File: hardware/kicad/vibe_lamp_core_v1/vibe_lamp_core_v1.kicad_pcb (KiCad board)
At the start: 2 copper layers, 32 x 32 mm, 27 parts, among them J1 USB-C_SMD-TYPE-C-31-M-12_1, P1 PinHeader_1x03_P2.54mm_Vertic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, SW1 Panasonic_EVQPUJ_EVQPUA, U1 WIFIM-SMD_ESP32-C3-MINI-1, U2 SOT-25-5_L2.9-W1.6-P0.95-LS2.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

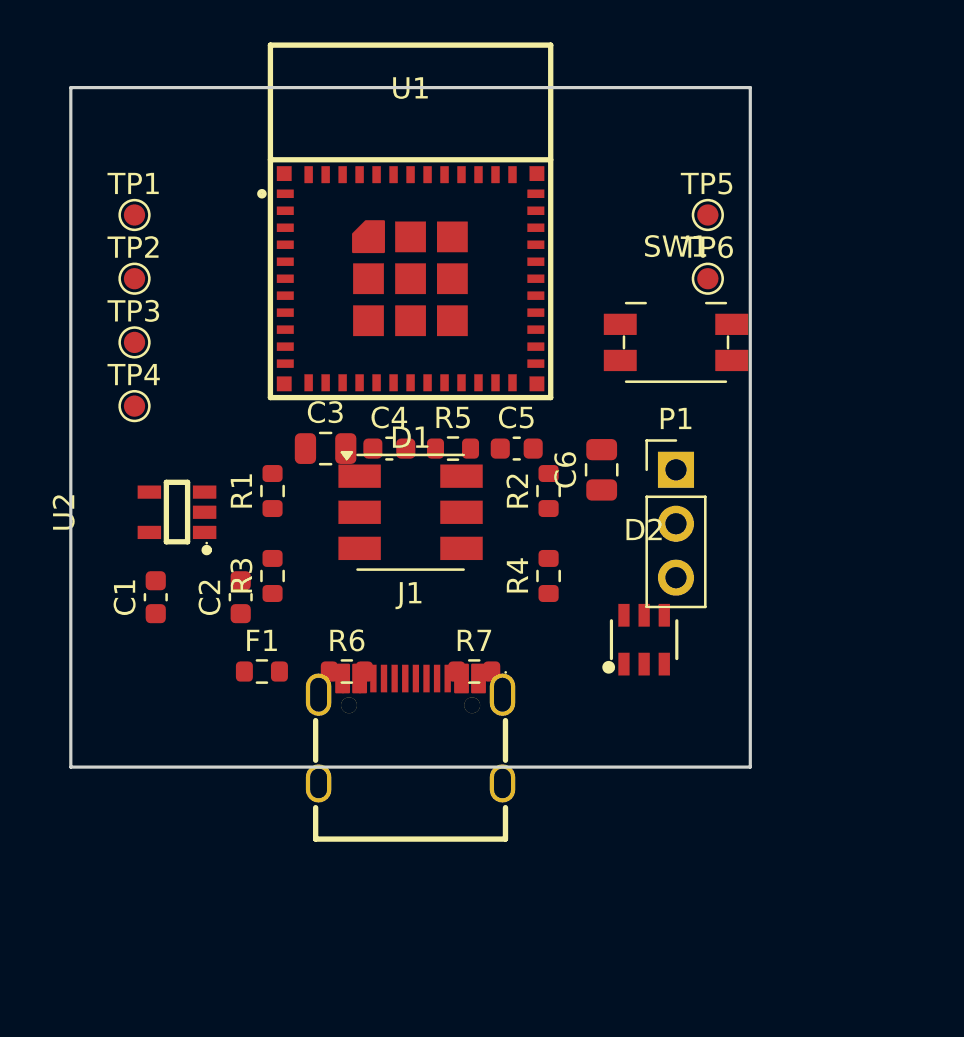
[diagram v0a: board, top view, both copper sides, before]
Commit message: wip(hardware): Core V1 auto-routed draft (Freerouting) + routing status
Auto-routed the placed board with Freerouting v1.9.0 (~75%, 64/86 connections) + dual-layer GND pour. NOT fab-ready: 21 unrouted, 4 shorts, 17 antenna-keepout intrusions, 9 courtyard overlaps remain (see hardware/v1_routing_status.md). Reproducible pcbnew/DSN/SES scripts saved under scripts/. The clean placed+netlist base is commit 9fb418d.

Co-Authored-By: Claude Opus 4.8 (1M context) <noreply@anthropic.com>
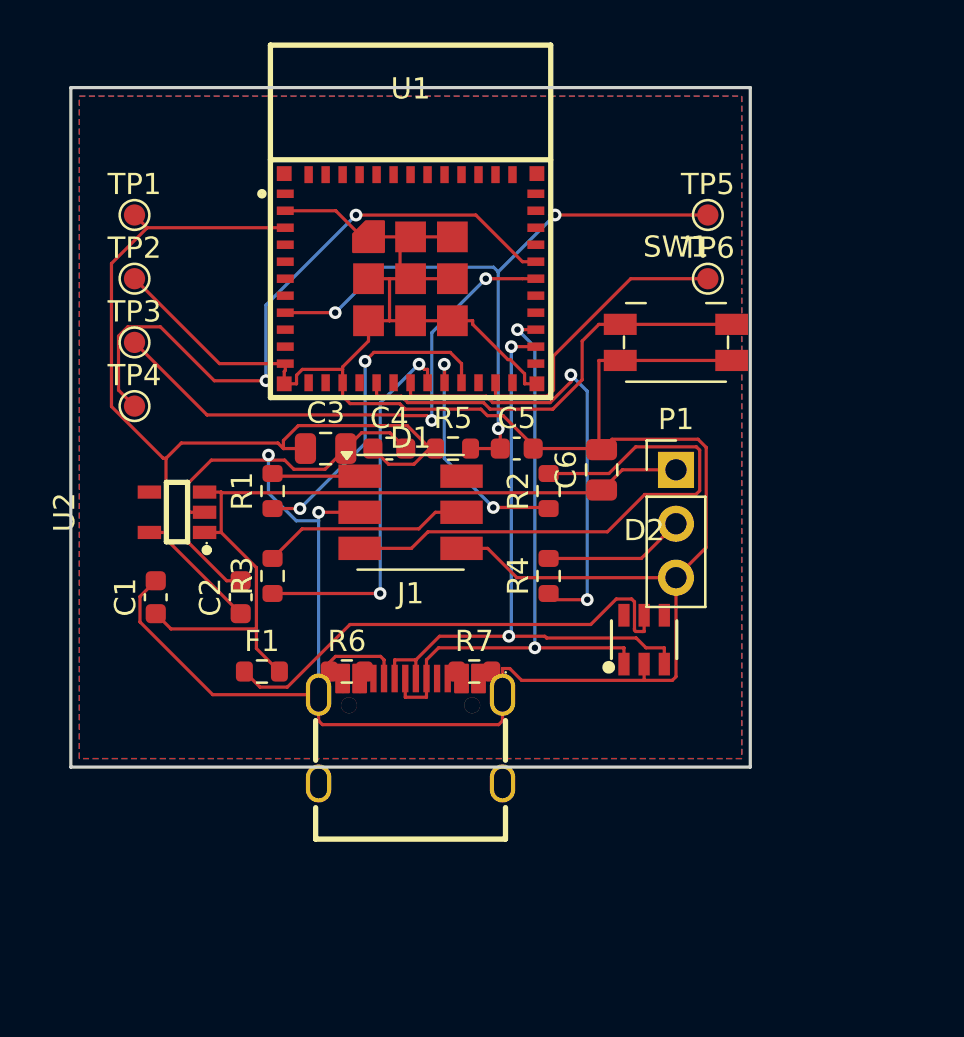
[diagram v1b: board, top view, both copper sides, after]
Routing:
- net GND: track 0.00 -> 163.3 mm, vias 0 -> 2
- net +3V3: track 0.00 -> 48.2 mm
- net +5V: track 0.00 -> 38.1 mm
- net EN: track 0.00 -> 31.7 mm, vias 0 -> 3
- net USB_DM: track 0.00 -> 30.8 mm, vias 0 -> 2
- net UART_TX: track 0.00 -> 30.7 mm, vias 0 -> 2
- net USB_DP: track 0.00 -> 30.1 mm, vias 0 -> 2
- net RGB_G: track 0.00 -> 26.8 mm
- net UART_RX: track 0.00 -> 25.6 mm, vias 0 -> 2
- net VBUS: track 0.00 -> 23.0 mm
- net IO4: track 0.00 -> 21.9 mm, vias 0 -> 2
- net BTN: track 0.00 -> 20.3 mm
- net IO5: track 0.00 -> 17.8 mm, vias 0 -> 2
- net IO7: track 0.00 -> 15.3 mm, vias 0 -> 2
- net IO9: track 0.00 -> 13.9 mm
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- added copper zone on B.Cu, net GND
- added copper zone on F.Cu, net GND

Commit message: feat(hardware): Core V1 clean 40x40 routed board (0 shorts, 1 unrouted)
Re-laid out on a 40x40 board with proper spacing and re-routed with Freerouting (100 passes) + dual-layer GND pour. From 86 violations/21 unconnected/4 shorts down to 23 violations/1 unconnected/0 shorts. Remaining are minor/tunable (tight clearances, GND thermals, silk, 1 unrouted net). Near fab-ready; final cleanup = relax clearance to JLCPCB spec, route 1 net, thermal tweak, then Gerber/BOM/CPL. See hardware/v1_routing_status.md.

Co-Authored-By: Claude Opus 4.8 (1M context) <noreply@anthropic.com>
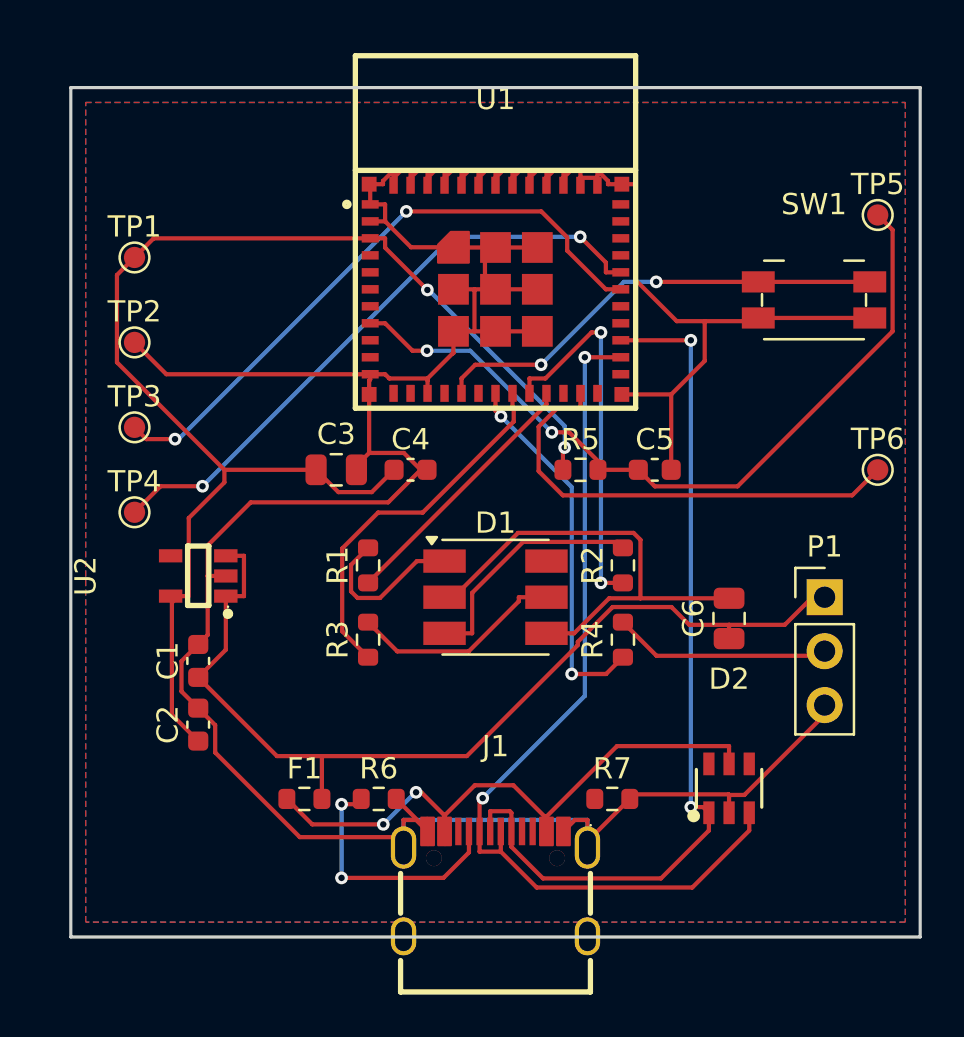
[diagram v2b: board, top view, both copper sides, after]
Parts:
- moved TP6 12.0 mm to (38.0, 18.0)
- moved C6 9.22 mm to (31.0, 25.0)
- moved P1 9.22 mm to (35.5, 24.0)
- moved R7 8.85 mm to (25.5, 33.5)
- moved J1 8.24 mm to (20.0, 37.5)
- moved D2 8.06 mm to (31.0, 33.0)
- moved TP5 8.00 mm to (38.0, 6.00)
- moved SW1 6.80 mm to (35.0, 10.0)
- moved C5 6.58 mm to (27.5, 18.0)
- moved C2 6.32 mm to (6.00, 30.0)
- moved F1 6.32 mm to (11.0, 33.5)
- moved R6 6.18 mm to (14.5, 33.5)
- moved R5 6.08 mm to (24.0, 18.0)
- moved R1 5.70 mm to (14.0, 22.5)
- moved D1 5.66 mm to (20.0, 24.0)
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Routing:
- net GND: track 163.3 -> 189.0 mm, vias 2 -> 0
- net RGB_G: track 26.8 -> 11.4 mm
- net +3V3: track 48.2 -> 62.9 mm, vias 0 -> 2
- net USB_DM: track 30.8 -> 43.3 mm
- net USB_DP: track 30.1 -> 41.5 mm
- net IO9: track 13.9 -> 22.1 mm
- net CC1: track 4.07 -> 12.0 mm, vias 0 -> 2
- net +5V: track 38.1 -> 45.6 mm
- net IO6: track 11.2 -> 17.8 mm
- net EN: track 31.7 -> 36.8 mm, vias 3 -> 2
- net IO4: track 21.9 -> 17.4 mm
- net VBUS: track 23.0 -> 27.3 mm, vias 0 -> 2
- net UART_RX: track 25.6 -> 29.5 mm
- net WS_DATA: track 6.68 -> 10.2 mm
- net RGB_R: track 4.15 -> 7.64 mm
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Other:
- board size 32 x 32 mm -> 40 x 40 mm

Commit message: feat(hardware): Core V1 fab outputs (Gerber/drill/BOM/CPL) + component values
Set real component values; export JLCPCB-ready Gerber+drill zip, BOM (U1/U2/J1/D2 with LCSC), and CPL placement under fab/. Board is 0 shorts, 1 unrouted net (CC2) — a draft; see v1_routing_status.md for the pre-order checklist (route CC2, fill passive LCSC, clear connector-inherent DRC).

Co-Authored-By: Claude Opus 4.8 (1M context) <noreply@anthropic.com>
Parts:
- C1, C2: value C_0603_1608Metric -> 1uF
- C3: value C_0805_2012Metric -> 10uF
- C4, C5: value C_0603_1608Metric -> 100nF
- C6: value C_0805_2012Metric -> 470uF
- D1: value LED_RGB_5050-6 -> RGB-LED-5050-CC
- D2: value SOT-23-6_L2.9-W1.6-P0.95-LS2.8-BL -> USBLC6-2SC6
- F1: value R_0603_1608Metric -> 0R
- J1: value USB-C_SMD-TYPE-C-31-M-12_1 -> USB-C-TYPE-C-31-M-12
- P1: value PinHeader_1x03_P2.54mm_Vertical -> WS2812-EXT-1x3
- R1: value R_0603_1608Metric -> 470
- R2, R3: value R_0603_1608Metric -> 150
- R4: value R_0603_1608Metric -> 330
- R5: value R_0603_1608Metric -> 10k
- R6, R7: value R_0603_1608Metric -> 5.1k
- SW1: value Panasonic_EVQPUJ_EVQPUA -> SW-PUSH
- U1: value WIFIM-SMD_ESP32-C3-MINI-1 -> ESP32-C3-MINI-1
- U2: value SOT-25-5_L2.9-W1.6-P0.95-LS2.8-BL -> AP2112K-3.3
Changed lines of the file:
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@@
 			)
 		)
-		(property "Value" "PinHeader_1x03_P2.54mm_Vertical"
+		(property "Value" "WS2812-EXT-1x3"
 			(at 0 7.46 0)
 			(layer "F.Fab")
@@
 			)
 		)
-		(property "Value" "R_0603_1608Metric"
+		(property "Value" "5.1k"
 			(at 0 1.43 0)
 			(layer "F.Fab")
@@
 			)
 		)
-		(property "Value" "C_0603_1608Metric"
+		(property "Value" "1uF"
 			(at 0 1.43 90)
 			(layer "F.Fab")
@@
 			)
 		)
-		(property "Value" "C_0805_2012Metric"
+		(property "Value" "470uF"
 			(at 0 1.68 90)
 			(layer "F.Fab")
@@
 			)
 		)
-		(property "Value" "C_0603_1608Metric"
+		(property "Value" "100nF"
 			(at 0 1.43 0)
 			(layer "F.Fab")
@@
 			)
 		)
-		(property "Value" "R_0603_1608Metric"
+		(property "Value" "0R"
 			(at 0 1.43 0)
 			(layer "F.Fab")
@@
 			)
 		)
-		(property "Value" "C_0603_1608Metric"
+		(property "Value" "1uF"
 			(at 0 1.43 90)
 			(layer "F.Fab")
@@
 			)
 		)
-		(property "Value" "SOT-25-5_L2.9-W1.6-P0.95-LS2.8-BL"
+		(property "Value" "AP2112K-3.3"
 			(at 0 5.3 90)
 			(layer "F.Fab")
@@
 			)
 		)
-		(property "Value" "R_0603_1608Metric"
+		(property "Value" "150"
 			(at 0 1.43 90)
 			(layer "F.Fab")
@@
 			)
 		)
-		(property "Value" "R_0603_1608Metric"
+		(property "Value" "10k"
 			(at 0 1.43 0)
 			(layer "F.Fab")
@@
 			)
 		)
-		(property "Value" "LED_RGB_5050-6"
+		(property "Value" "RGB-LED-5050-CC"
 			(at 0 3.3 0)
 			(layer "F.Fab")
@@
 			)
 		)
-		(property "Value" "C_0805_2012Metric"
+		(property "Value" "10uF"
 			(at 0 1.68 0)
 			(layer "F.Fab")
@@
 			)
 		)
-		(property "Value" "C_0603_1608Metric"
+		(property "Value" "100nF"
 			(at 0 1.43 0)
 			(layer "F.Fab")
@@
 			)
 		)
-		(property "Value" "USB-C_SMD-TYPE-C-31-M-12_1"
+		(property "Value" "USB-C-TYPE-C-31-M-12"
 			(at 0 6.474 0)
 			(layer "F.Fab")
@@
 			)
 		)
-		(property "Value" "SOT-23-6_L2.9-W1.6-P0.95-LS2.8-BL"
+		(property "Value" "USBLC6-2SC6"
 			(at 0 5.149 0)
 			(layer "F.Fab")
@@
 			)
 		)
-		(property "Value" "WIFIM-SMD_ESP32-C3-MINI-1"
+		(property "Value" "ESP32-C3-MINI-1"
 			(at 0 8.95 0)
 			(layer "F.Fab")
@@
 			)
 		)
-		(property "Value" "R_0603_1608Metric"
+		(property "Value" "150"
 			(at 0 1.43 90)
 			(layer "F.Fab")
@@
 			)
 		)
-		(property "Value" "R_0603_1608Metric"
+		(property "Value" "470"
 			(at 0 1.43 90)
 			(layer "F.Fab")
@@
 			)
 		)
-		(property "Value" "R_0603_1608Metric"
+		(property "Value" "330"
 			(at 0 1.43 90)
 			(layer "F.Fab")
@@
 			)
 		)
-		(property "Value" "R_0603_1608Metric"
+		(property "Value" "5.1k"
 			(at 0 1.43 0)
 			(layer "F.Fab")
@@
 			)
 		)
-		(property "Value" "Panasonic_EVQPUJ_EVQPUA"
+		(property "Value" "SW-PUSH"
 			(at 0 3.5 0)
 			(layer "F.Fab")

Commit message: feat(hardware): route CC2, fix USB-C edge fit, add "vibe lamp" silk, fab re-export
Core V1 PCB finishing pass — board is now electrically complete:
- CC2 routed: moved R7 (CC2 pulldown) into the clear lane due-north of
  J1.B5 so CC2 is a straight 1.41mm trace (Freerouting deprioritized it).
  scripts/route_cc2.py auto-adds it. Result: 0 shorts, 0 unconnected.
- J1 (USB-C) shifted up 1.2mm so all pads sit on-board (shell still
  overhangs the edge for cable insertion); opened the connector fan-out
  pocket to ~3.8mm by moving the bottom passive row up.
- Branding silkscreen "vibe lamp" on front + back, "v1" on back.
- Design rules set to JLCPCB process (copper-to-edge 0.2mm, clearance
  0.127mm). DRC: 0 short / 0 unconnected / 20 minor (10 USB-C connector
  -inherent + 8 cosmetic silk + courtyard + thermal).
- Re-exported all fab outputs; fixed gerber zip to include the actual
  manufacturing layers (copper/mask/silk/edge/paste/drill) — the prior
  zip glob (*.gbr) had silently dropped them. Dropped non-fab layers.
- BOM: verified LCSC parts against JLCPCB library. U1/U2/J1/D2 filled.
  D1 needs a selection decision (6-pin 5050 analog CC RGB has no clean
  JLCPCB stock match — see v1_routing_status.md); SW1 + passives guided.

Co-Authored-By: Claude Opus 4.8 (1M context) <noreply@anthropic.com>
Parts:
- moved R7 4.20 mm to (21.8, 31.6), turned to 90 degrees
- moved R6 3.81 mm to (13.0, 30.0)
- moved F1 3.64 mm to (10.0, 30.0)
- moved D2 3.00 mm to (31.0, 30.0)
- moved J1 1.20 mm to (20.0, 36.3)
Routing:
- net GND: track 189.0 -> 248.9 mm, vias 0 -> 1
- net UART_TX: track 29.2 -> 45.1 mm, vias 2 -> 0
- net EN: track 36.8 -> 44.8 mm
- net +3V3: track 62.9 -> 56.0 mm, vias 2 -> 0
- net IO4: track 17.4 -> 24.3 mm
- net BTN: track 21.8 -> 28.1 mm
- net IO9: track 22.1 -> 15.9 mm
- net IO5: track 17.5 -> 22.5 mm, vias 0 -> 2
- net IO6: track 17.8 -> 13.8 mm
- net RGB_R: track 7.64 -> 3.86 mm
- net UART_RX: track 29.5 -> 26.0 mm
- net IO7: track 12.4 -> 15.0 mm, vias 0 -> 2
- net USB_DP: track 41.5 -> 39.4 mm
- net CC1: track 12.0 -> 13.5 mm
- net CC2: track 0.00 -> 1.41 mm
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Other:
- board text added: "v1"
- board text added: "vibe lamp"

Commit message: feat(hardware,firmware): switch D1 to WS2812B, finalize Core V1 BOM
D1 part-selection decision: 6-pin analog 5050 common-cathode RGB has no
in-stock JLCPCB match, so switch the onboard LED to WS2812B (digital).

Hardware (Core V1 PCB):
- D1 -> WS2812B (LCSC C2761795, SMD5050-4P, 550k stock). Imported exact
  footprint via easyeda2kicad; pinout verified VDD/DOUT/VSS/DIN.
- Data chain GPIO4 -> R4(330) -> D1.DIN; D1.DOUT -> P1 (onboard LED is
  chain head, P1 cascades an external strip).
- Removed R1/R2/R3 (no RGB current-limit needed); added C7 100nF decap.
- SW1 -> SKRPABE010 (LCSC C115360) with its exact imported footprint.
- ESP32-C3-MINI-1 module pin->GPIO map verified against symbol: pin16=IO10
  (button), pin18=IO4 (WS data), pin26/27=IO18/19 (USB D-/D+), 3V3/EN/GND
  all correct.
- DRC: 0 short / 0 unconnected / 18 minor (10 USB-C connector-inherent +
  8 cosmetic silk). Rules set to JLCPCB process incl. min_resolved_spokes=1.
- Re-exported gerber/drill/cpl; BOM now has 6/6 key LCSC parts filled
  (U1/U2/J1/D2/D1/SW1); C6/P1 marked DNP; passives auto-match basic lib.

Firmware (additive, does NOT touch the working analog dev board):
- New env c3_core_v1: WS2812 single-LED (DISPLAY_WS2812_STRIP, NUM_LEDS=1,
  PIN_WS2812=4, PIN_RESET_BTN=10). Builds clean.
- config.h: make NUM_LEDS overridable via -DNUM_LEDS.
- Existing c3_rgb (analog RGB on GPIO5/6/7) unchanged; verified still builds.

Co-Authored-By: Claude Opus 4.8 (1M context) <noreply@anthropic.com>
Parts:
- removed R1: 470, R_0603_1608Metric
- removed R2, R3: 150, R_0603_1608Metric
- added C7: 100nF, C_0603_1608Metric, F.Cu at (14.0, 24.0)
- D1: value RGB-LED-5050-CC -> WS2812B; footprint LED_RGB_5050-6 -> LED-SMD_4P-L5.0-W5.0-TL_WS2812B-B
- SW1: footprint Panasonic_EVQPUJ_EVQPUA -> KEY-SMD_4P-L4.2-W3.2-P2.20-LS4.6
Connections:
- D1 pad 1: RGB_R -> +5V
- D1 pad 2: GND -> WS_DOUT
- D1 pad 3: RGB_G -> GND
- D1 pad 4: GND -> WS_DIN
- P1 pad 2: WS_DATA -> WS_DOUT
- R4 pad 2: WS_DATA -> WS_DIN
- U1 pad 19: IO5 -> (no net)
- U1 pad 20: IO6 -> (no net)
- U1 pad 21: IO7 -> (no net)
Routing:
- net IO5: track 22.5 -> 0.00 mm, vias 2 -> 0
- net WS_DOUT: track 0.00 -> 19.6 mm
- net WS_DIN: track 0.00 -> 18.8 mm
- net UART_RX: track 26.0 -> 41.9 mm, vias 2 -> 0
- net IO7: track 15.0 -> 0.00 mm, vias 2 -> 0
- net IO6: track 13.8 -> 0.00 mm, vias 2 -> 0
- net UART_TX: track 45.1 -> 33.5 mm, vias 0 -> 2
- net RGB_G: track 11.4 -> 0.00 mm
- net WS_DATA: track 10.2 -> 0.00 mm
- net RGB_B: track 10.2 -> 0.00 mm
- net EN: track 44.8 -> 36.7 mm, vias 2 -> 0
- net BTN: track 28.1 -> 20.0 mm, vias 2 -> 0
- net IO9: track 15.9 -> 23.8 mm, vias 0 -> 2
- net RGB_R: track 3.86 -> 0.00 mm
- net GND: track 248.9 -> 245.8 mm, vias 1 -> 0
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
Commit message: feat(hardware): add D3 (1N4148WS) level-margin diode for WS2812B data
WS2812B DIN high threshold = 0.7*VDD = 3.5V at 5V, above the ESP32-C3's
3.3V GPIO (marginal). Add series diode D3 (1N4148WS, LCSC C2128, JLCPCB
Basic, 2.4M stock) dropping D1's supply 5V -> ~4.3V (new net LED5V), so
the threshold falls to ~3.0V and 3.3V data is solidly in spec. External
strip header P1 stays on full +5V. Fully PCBA, no hand-soldering.

- D3.A -> +5V, D3.K -> LED5V -> D1.VDD + C7 decap.
- DRC: 0 short / 0 unconnected / 19 minor (10 connector-inherent + 9
  cosmetic silk). BOM now 7/7 key LCSC parts filled; gerber/cpl/bom re-exported.

Co-Authored-By: Claude Opus 4.8 (1M context) <noreply@anthropic.com>
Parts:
- added D3: 1N4148WS, SOD-323_L1.8-W1.3-LS2.5-RD, F.Cu at (17.0, 20.0)
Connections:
- C7 pad 1: +5V -> LED5V
- D1 pad 1: +5V -> LED5V
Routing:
- net WS_DIN: track 18.8 -> 4.91 mm
- net GND: track 245.8 -> 234.4 mm, vias 0 -> 1
- net IO9: track 23.8 -> 15.9 mm
- net LED5V: track 0.00 -> 7.15 mm
- net IO4: track 22.3 -> 16.1 mm
- net EN: track 36.7 -> 42.7 mm, vias 0 -> 2
- net USB_DM: track 42.4 -> 46.0 mm
- net UART_TX: track 33.5 -> 31.3 mm
- net CC1: track 13.5 -> 11.9 mm
- net +3V3: track 56.6 -> 58.2 mm
- net BTN: track 20.0 -> 19.6 mm, vias 0 -> 2
